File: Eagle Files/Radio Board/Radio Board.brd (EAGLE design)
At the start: 33 x 33 mm, 16 parts, among them Y2 16 MHZ

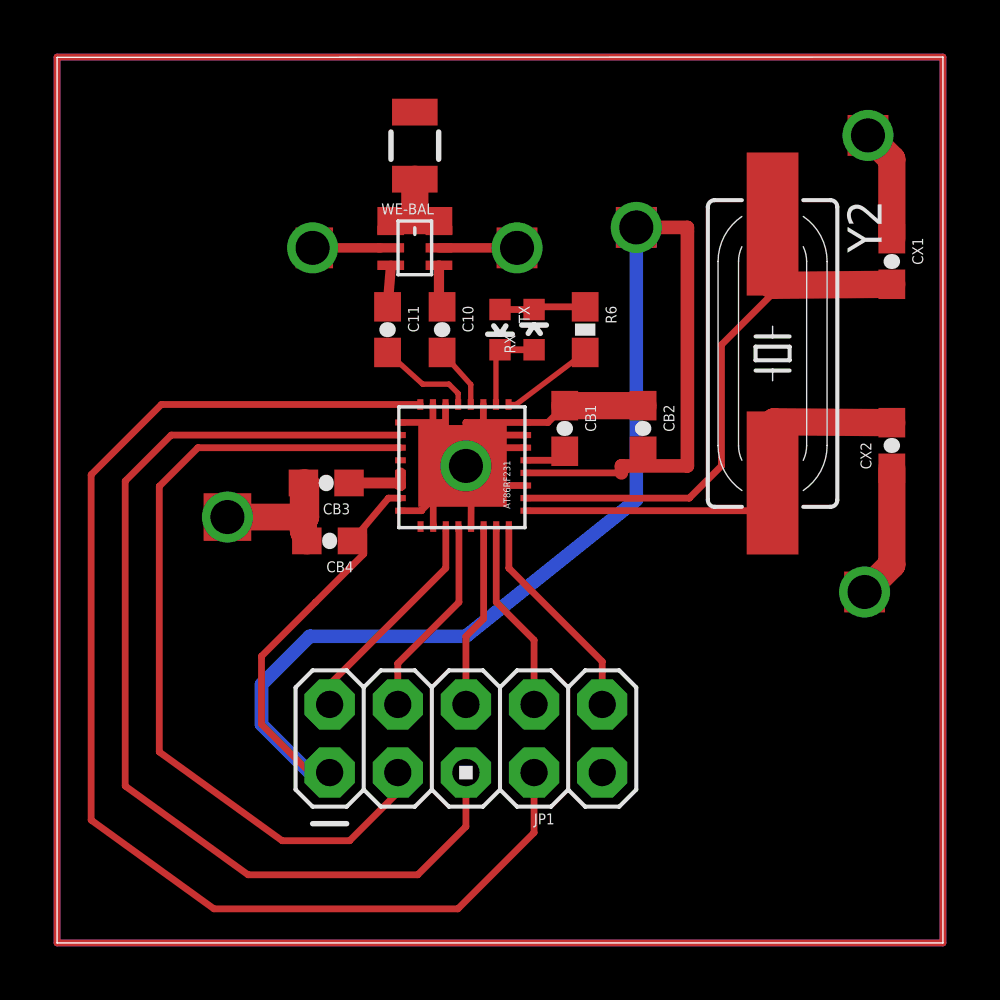
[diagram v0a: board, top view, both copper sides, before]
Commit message: Radio Board now has pull up resistors on Radio Reset, and Radio CS.
--Arthur

git-svn-id: http://cd-net.net/CPE496/trunk@90 05b6d0e0-c345-4a8e-a5b7-579c8bd0b646
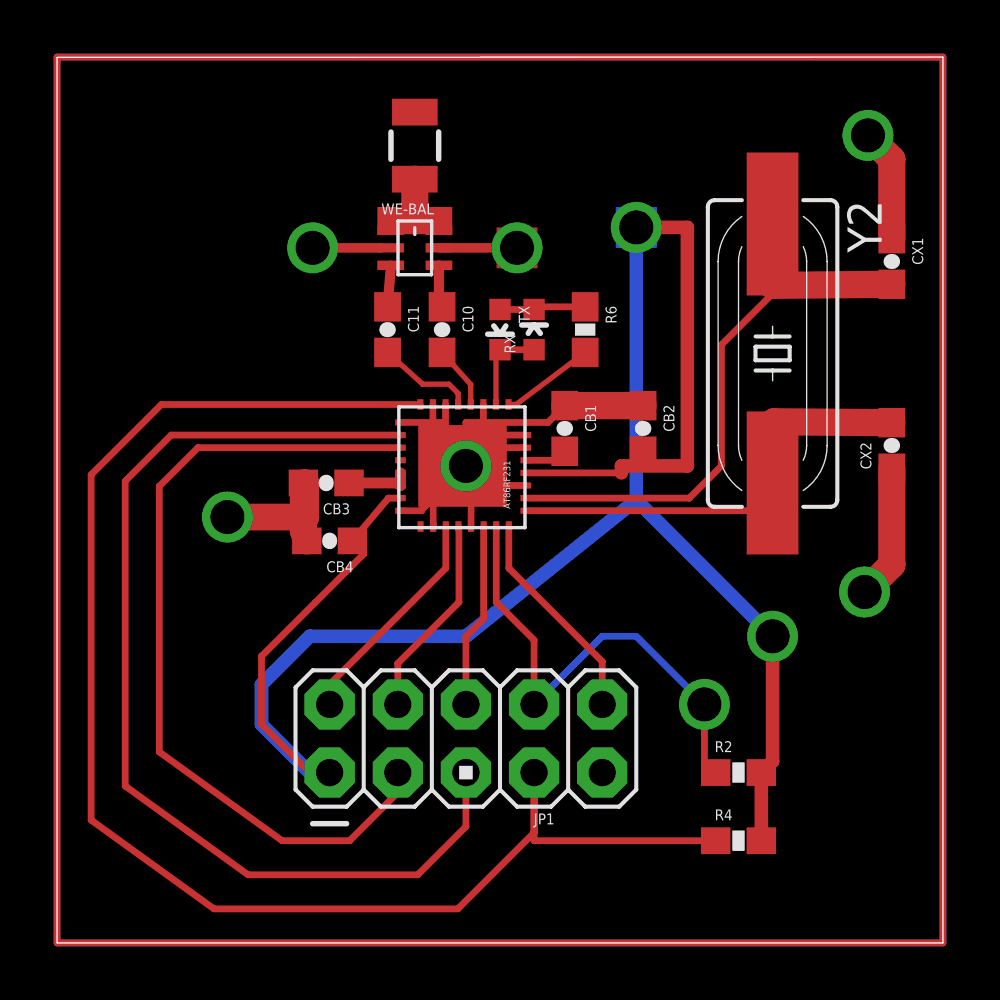
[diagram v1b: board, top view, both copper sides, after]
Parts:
- added R2, R4: 10K, SparkFun:0603-RES
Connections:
- net 3.3V: now also R2.2, R4.2
- net CS-RADIO: now also R2.1
- net RADIO-RST: now also R4.1
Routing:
- net 3.3V: track 64.6 -> 79.6 mm, vias 1 -> 2
- net CS-RADIO: track 7.21 -> 18.6 mm, vias 0 -> 1
- net RADIO-RST: track 47.2 -> 56.5 mm
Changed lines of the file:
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@@
 <rectangle x1="12.827" y1="25.527" x2="13.843" y2="28.321" layer="1" rot="R90"/>
 <rectangle x1="13.462" y1="16.256" x2="16.764" y2="19.304" layer="1"/>
-<rectangle x1="5.461" y1="14.986" x2="7.239" y2="16.764" layer="1"/>
-<rectangle x1="8.89" y1="25.146" x2="10.287" y2="26.67" layer="1"/>
 <rectangle x1="16.383" y1="25.146" x2="17.907" y2="26.67" layer="1"/>
-<rectangle x1="20.828" y1="25.908" x2="22.352" y2="27.432" layer="1"/>
-<rectangle x1="29.337" y1="12.319" x2="30.861" y2="13.843" layer="1"/>
-<rectangle x1="9.652" y1="8.382" x2="10.795" y2="9.398" layer="1"/>
-<rectangle x1="12.192" y1="8.255" x2="13.208" y2="9.398" layer="1"/>
-<rectangle x1="14.605" y1="8.255" x2="15.875" y2="9.398" layer="1"/>
-<rectangle x1="17.272" y1="8.382" x2="18.288" y2="9.398" layer="1"/>
-<rectangle x1="19.812" y1="8.382" x2="20.828" y2="9.525" layer="1"/>
-<rectangle x1="19.812" y1="5.842" x2="20.955" y2="6.858" layer="1"/>
-<rectangle x1="17.272" y1="5.842" x2="18.415" y2="6.858" layer="1"/>
-<rectangle x1="14.605" y1="5.842" x2="15.875" y2="6.858" layer="1"/>
-<rectangle x1="12.192" y1="5.842" x2="13.208" y2="6.858" layer="1"/>
-<rectangle x1="9.652" y1="5.842" x2="10.668" y2="6.858" layer="1"/>
 <rectangle x1="20.828" y1="25.908" x2="22.352" y2="27.432" layer="16"/>
 <rectangle x1="9.652" y1="8.382" x2="10.795" y2="9.398" layer="16"/>
@@
 <rectangle x1="12.065" y1="5.842" x2="13.335" y2="6.858" layer="16"/>
 <rectangle x1="9.652" y1="5.842" x2="10.668" y2="6.858" layer="16"/>
-<rectangle x1="29.464" y1="29.337" x2="30.988" y2="30.861" layer="1"/>
 </plain>
 <attributes>
@@
 <element name="U$5" library="SparkFun" package="ANTENNA-CHIP2" value="ANTENNA2SMD" x="13.335" y="29.718" rot="R180"/>
 <element name="JP1" library="SparkFun" package="AVR_ICSP" value="M05X2PTH" x="15.24" y="7.62" rot="R90"/>
+<element name="R2" library="SparkFun" package="0603-RES" value="10K" x="25.4" y="6.35"/>
+<element name="R4" library="SparkFun" package="0603-RES" value="10K" x="25.4" y="3.81"/>
 </elements>
 <signals>
@@
 <contactref element="U$4" pad="GNDDC"/>
 <contactref element="U$4" pad="GND"/>
-<polygon width="0.254" layer="16" isolate="0.508" thermals="no">
+<polygon width="0.254" layer="16" isolate="0.508" orphans="yes" thermals="no">
 <vertex x="33.02" y="33.02"/>
 <vertex x="0" y="33.02"/>
@@
 <wire x1="7.62" y1="8.14605" x2="9.41605" y2="6.35" width="0.508" layer="16"/>
 <wire x1="9.41605" y1="6.35" x2="10.16" y2="6.35" width="0.508" layer="16"/>
+<contactref element="R2" pad="2"/>
+<contactref element="R4" pad="2"/>
+<via x="26.67" y="11.43" extent="1-16" drill="1.27" shape="square"/>
+<wire x1="26.67" y1="11.43" x2="26.67" y2="6.77" width="0.508" layer="1"/>
+<wire x1="26.67" y1="6.77" x2="26.25" y2="6.35" width="0.508" layer="1"/>
+<wire x1="26.25" y1="6.35" x2="26.25" y2="3.81" width="0.508" layer="1"/>
+<wire x1="26.67" y1="11.43" x2="21.59" y2="16.51" width="0.508" layer="16"/>
 </signal>
 <signal name="SCK">
@@
 <wire x1="16.37" y1="12.7" x2="17.78" y2="11.29" width="0.254" layer="1"/>
 <wire x1="17.78" y1="11.29" x2="17.78" y2="8.89" width="0.254" layer="1"/>
+<contactref element="R2" pad="1"/>
+<via x="24.13" y="8.89" extent="1-16" drill="1.27" shape="square"/>
+<wire x1="24.55" y1="6.35" x2="24.13" y2="6.35" width="0.254" layer="1"/>
+<wire x1="24.13" y1="6.35" x2="24.13" y2="8.89" width="0.254" layer="1"/>
+<wire x1="24.13" y1="8.89" x2="22.86" y2="10.16" width="0.254" layer="16"/>
+<wire x1="22.86" y1="10.16" x2="21.59" y2="11.43" width="0.254" layer="16"/>
+<wire x1="21.59" y1="11.43" x2="20.32" y2="11.43" width="0.254" layer="16"/>
+<wire x1="20.32" y1="11.43" x2="17.78" y2="8.89" width="0.254" layer="16"/>
 </signal>
 <signal name="RADIO-RST">
@@
 <wire x1="14.94019375" y1="1.27" x2="17.78" y2="4.10980625" width="0.254" layer="1"/>
 <wire x1="17.78" y1="4.10980625" x2="17.78" y2="6.35" width="0.254" layer="1"/>
+<contactref element="R4" pad="1"/>
+<wire x1="24.55" y1="3.81" x2="17.78" y2="3.81" width="0.254" layer="1"/>
+<wire x1="17.78" y1="3.81" x2="17.78" y2="6.35" width="0.254" layer="1"/>
 </signal>
 <signal name="SLP_TR">

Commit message: Updated Boards
--Arthur

git-svn-id: http://cd-net.net/CPE496/trunk@93 05b6d0e0-c345-4a8e-a5b7-579c8bd0b646
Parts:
- moved CB1 0.18 mm to (19.1, 19.3)
- moved CB2 0.13 mm to (21.8, 19.3)
- moved R6 0.13 mm to (19.7, 23.0)
- moved RX 0.13 mm to (17.8, 23.0)
- moved TX 0.13 mm to (16.5, 23.0)

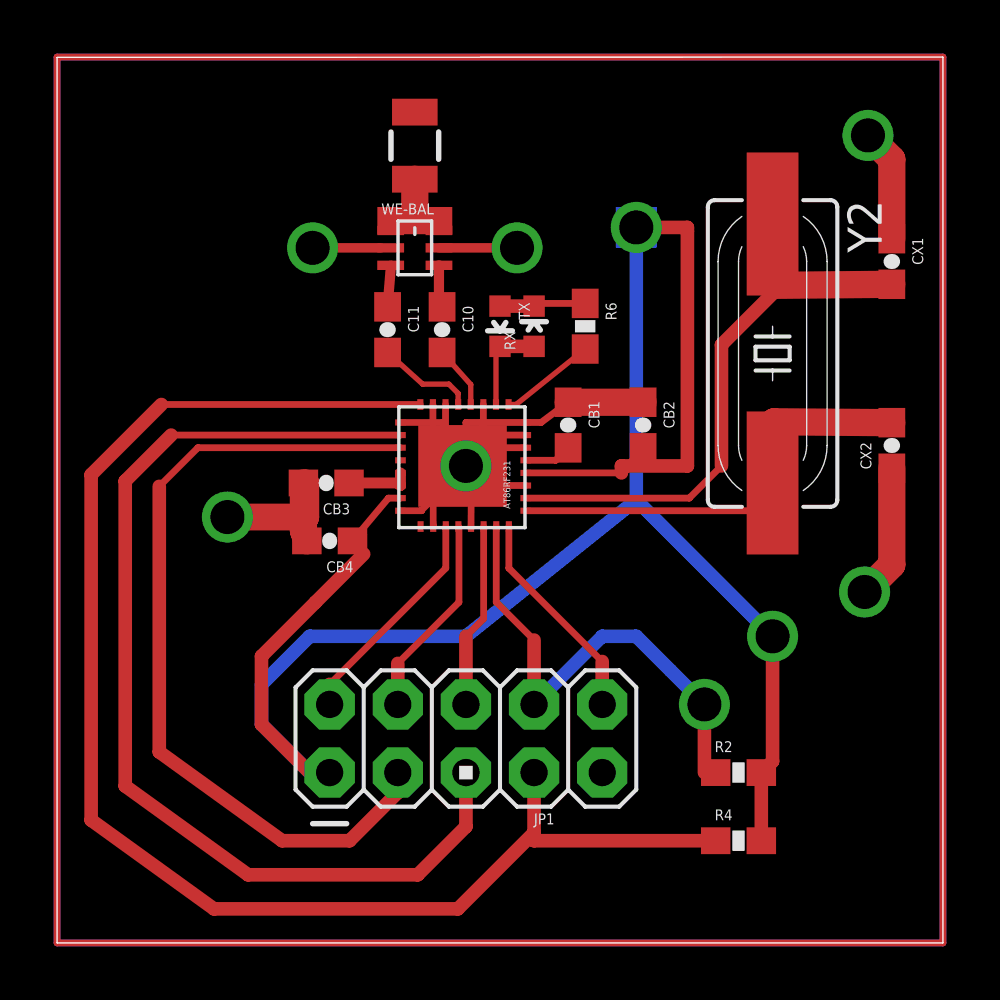
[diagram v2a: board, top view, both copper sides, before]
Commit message: Main Board with Headers is now almost ready.
I'm adding the FTDI Module right now.

TODO:
1.  Double check regulator Datasheet.  I think we're missing a capacitor.
2.  Update Radio Module Schematics to incorporate ground plane.
3.  Check if the hall effect sensor can work linearly at 3.3V
4.  Finish Adding FTDI chip and USB connector.

--Arthur

git-svn-id: http://cd-net.net/CPE496/trunk@119 05b6d0e0-c345-4a8e-a5b7-579c8bd0b646
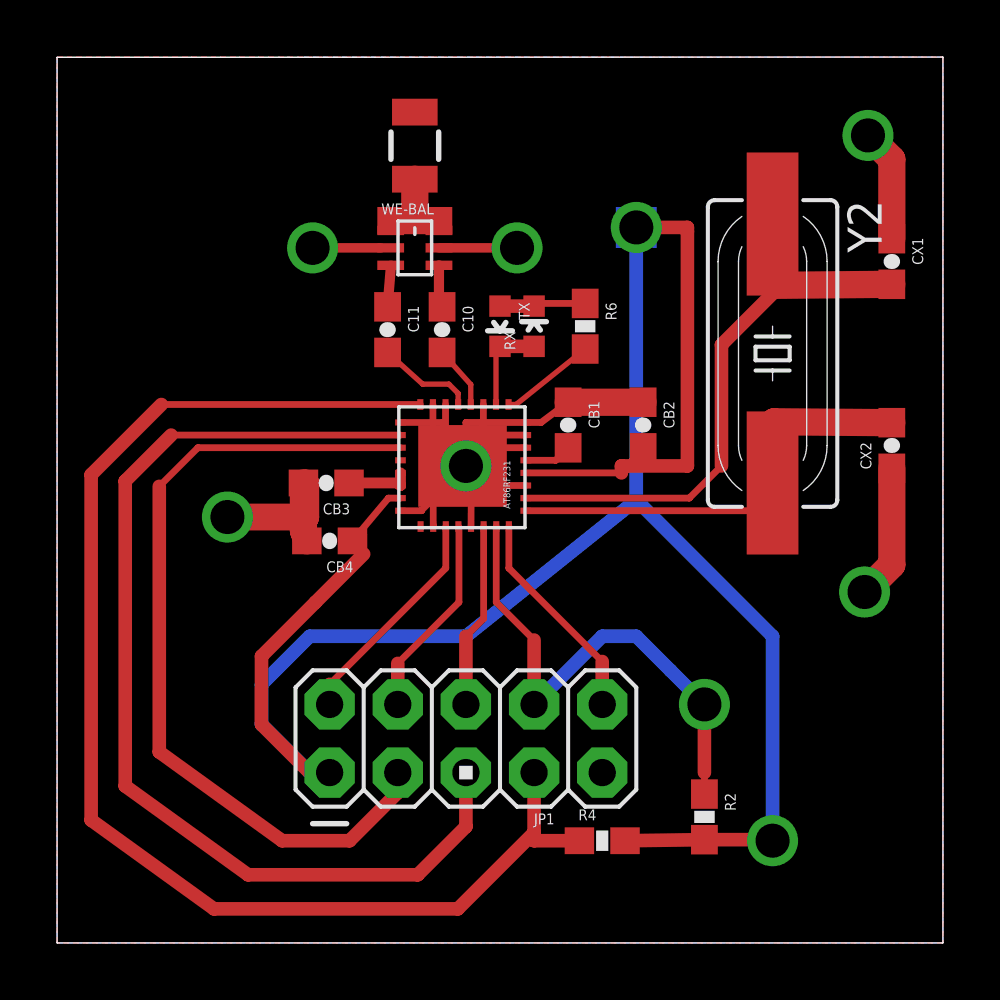
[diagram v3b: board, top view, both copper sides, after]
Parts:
- moved R4 5.08 mm to (20.3, 3.81)
- moved R2 2.08 mm to (24.1, 4.70), turned to 270 degrees
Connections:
- removed net CLKM: U$3.CLKM
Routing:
- net N$2: track 132.1 -> 0.00 mm
- net N$1: track 132.1 -> 0.00 mm
- net 3.3V: track 79.7 -> 85.1 mm
- net RADIO-RST: track 56.5 -> 51.5 mm
